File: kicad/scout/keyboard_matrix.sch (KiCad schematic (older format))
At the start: 17 parts, among them SW10 SPST, SW11 SPST, SW12 SPST, SW13 SPST, SW14 SPST, SW15 SPST, SW16 SPST, SW17 SPST, SW18 SPST, SW2 SPST, SW3 SPST, SW4 SPST, SW5 SPST, SW6 SPST, SW7 SPST, SW8 SPST, SW9 SPST

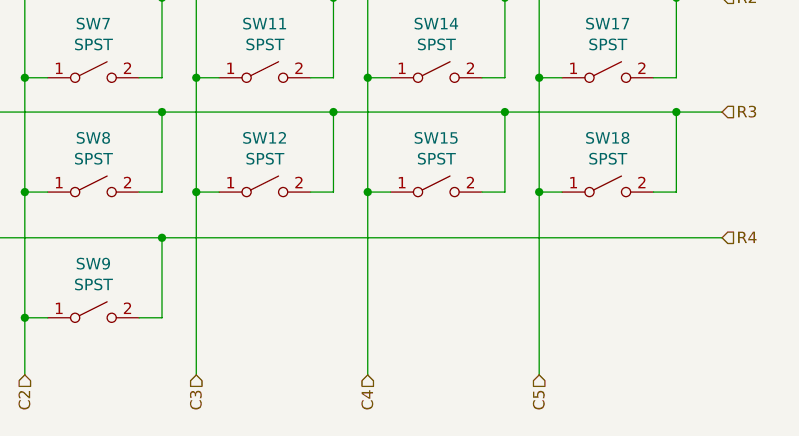
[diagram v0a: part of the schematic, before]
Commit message: PCB rev _b (private B)
* Increase mount length
* Move, right-angle (same footprint), flip to front, and reverse switch
* Move RGB LED, fix pin order, switch to easier footprint, and label GND
* Move FTDI and headphone jack for better exposure
* Add ICSP header
* Expose remaining ATMEGA pins and matrix buttons for hacking
* Add license, website, and plead
* Test SVG silkscreens -- fun!
* Mark relief hole to show which side it goes in
* Polarize C3 (amp gain) from ceramic to electrolytic
* Reverse volume direction
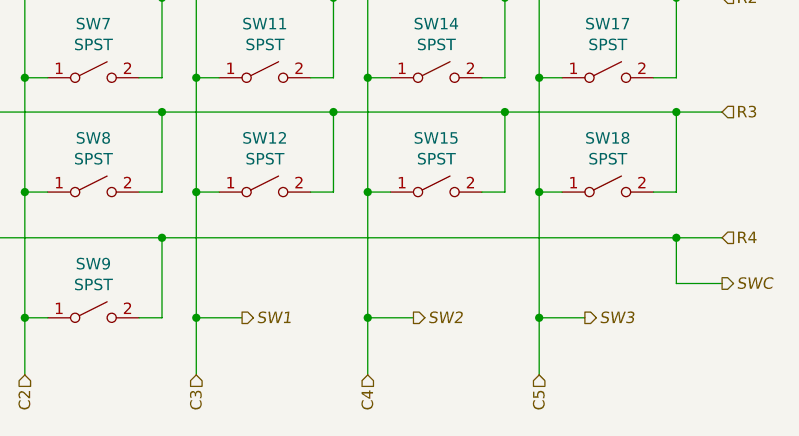
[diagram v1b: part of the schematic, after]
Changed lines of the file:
@@
 Connection ~ 7000 3850
 Wire Wire Line
-	4750 4400 7200 4400
+	4750 4400 7000 4400
 Connection ~ 4750 4400
 Wire Wire Line
@@
 Connection ~ 4150 4750
 Wire Wire Line
-	4900 4200 4900 5000
+	4900 4200 4900 4750
 Connection ~ 4900 4200
 Wire Wire Line
-	5650 4200 5650 5000
+	5650 4200 5650 4750
 Connection ~ 5650 4200
 Wire Wire Line
-	6400 4200 6400 5000
+	6400 4200 6400 4750
 Connection ~ 6400 4200
 Text HLabel 6400 5000 3    50   Input ~ 0
 C5
+Text HLabel 5100 4750 2    50   Output Italic 0
+SW1
+Text HLabel 5850 4750 2    50   Output Italic 0
+SW2
+Text HLabel 6600 4750 2    50   Output Italic 0
+SW3
+Wire Wire Line
+	4900 4750 5100 4750
+Connection ~ 4900 4750
+Wire Wire Line
+	4900 4750 4900 5000
+Wire Wire Line
+	5650 4750 5850 4750
+Connection ~ 5650 4750
+Wire Wire Line
+	5650 4750 5650 5000
+Wire Wire Line
+	6600 4750 6400 4750
+Connection ~ 6400 4750
+Wire Wire Line
+	6400 4750 6400 5000
+Text HLabel 7200 4600 2    50   Output Italic 0
+SWC
+Wire Wire Line
+	7000 4400 7000 4600
+Wire Wire Line
+	7000 4600 7200 4600
+Connection ~ 7000 4400
+Wire Wire Line
+	7000 4400 7200 4400
 $EndSCHEMATC

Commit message: Add schematic sheet corner text
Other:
- note added: "2020/07/16"
- note added: "A"
- note added: "Scout keyboard matrix"
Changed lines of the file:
@@
 Wire Wire Line
 	7000 4400 7200 4400
+Text Notes 7450 7500 0    50   ~ 0
+Scout keyboard matrix
+Text Notes 10600 7650 0    50   ~ 0
+A
+Text Notes 8150 7650 0    50   ~ 0
+2020/07/16
 $EndSCHEMATC

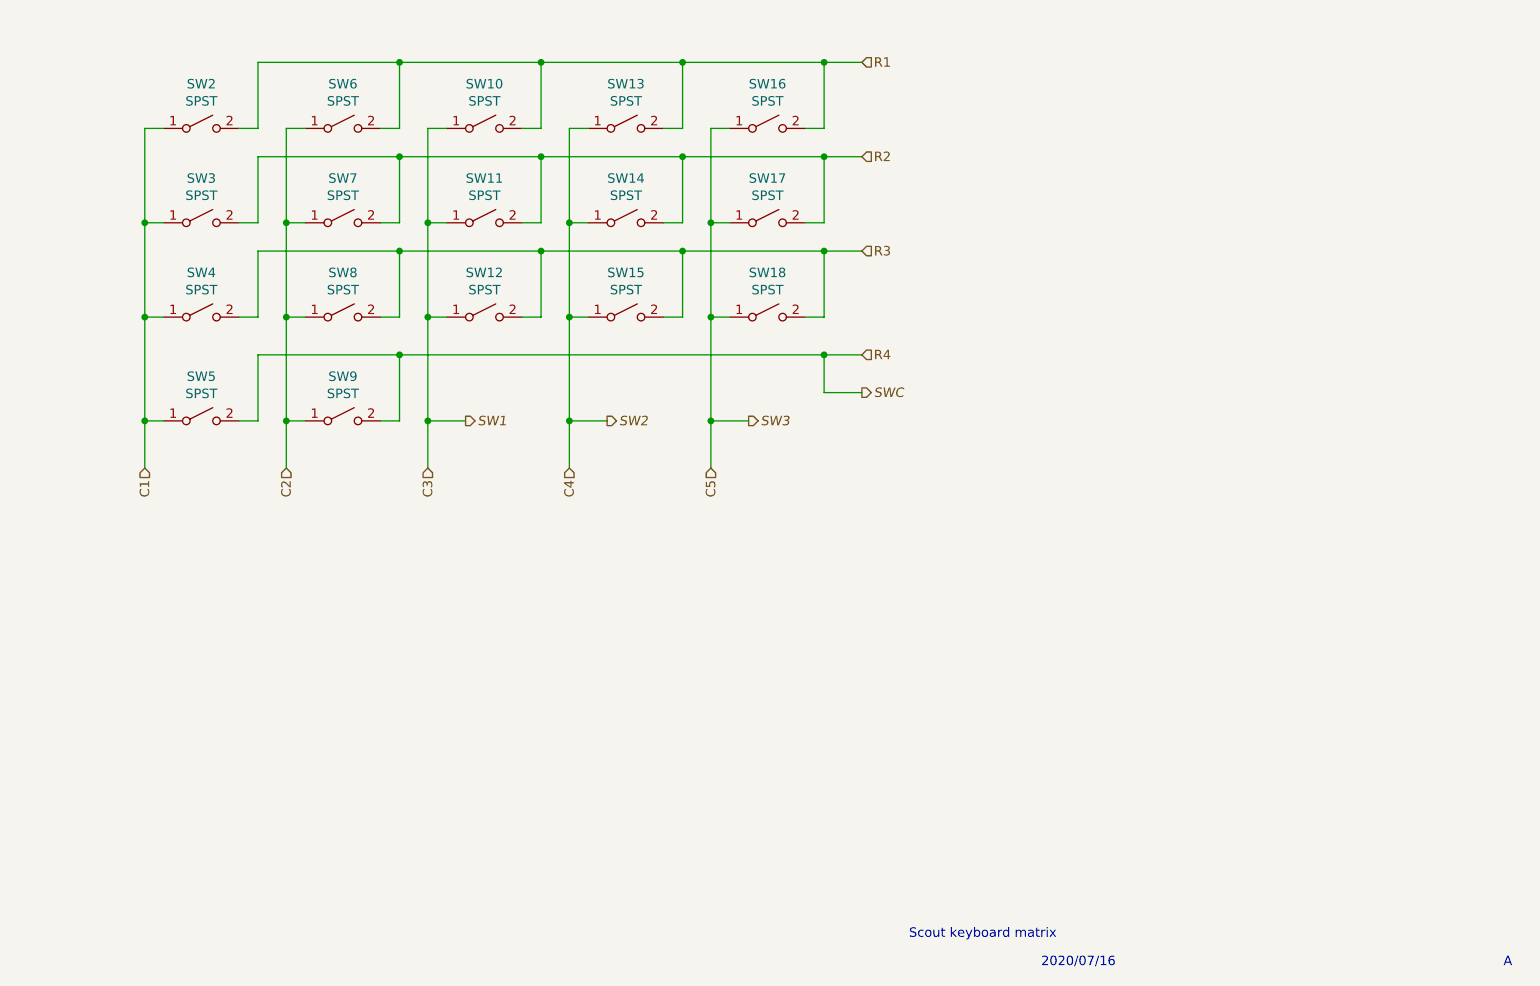
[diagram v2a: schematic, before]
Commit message: START Revise schematics
* Add all key switches with new diodes
* Swap pins 9 and 11 (re: MozziScout)
* Add two analog input pots
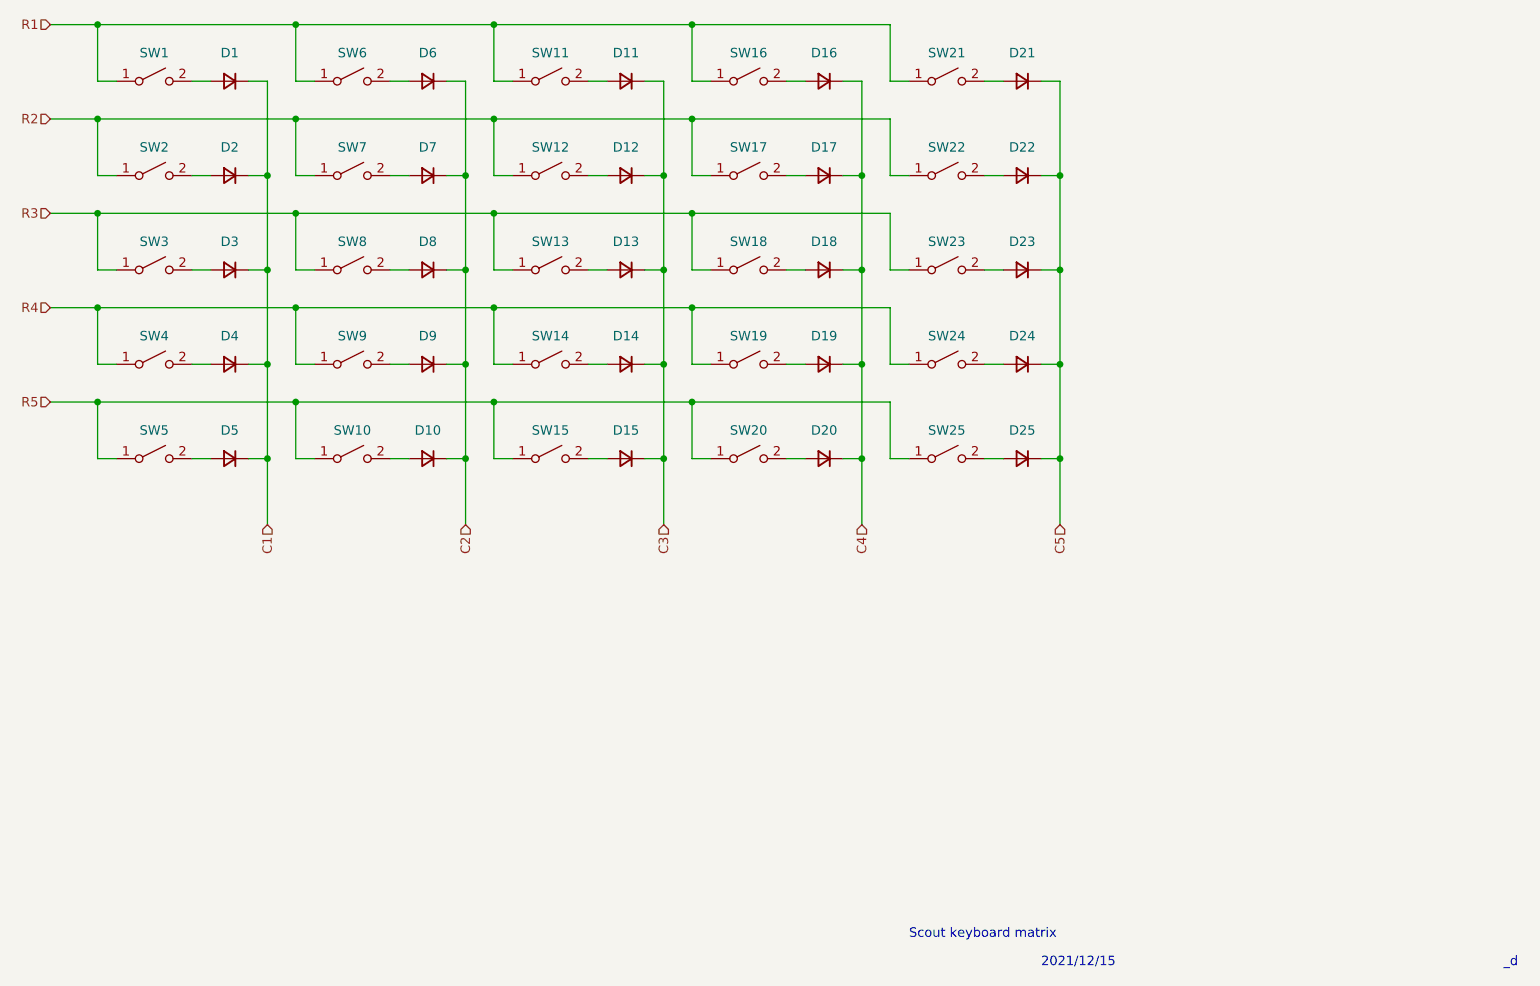
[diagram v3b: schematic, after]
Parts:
- added D1, D10, D11, D12, D13, D14, D15, D16, D17, D18, D19, D2, D20, D21, D22, D23, D24, D25, D3, D4, D5, D6, D7, D8, D9: D, symbol Device:D_Small
- added SW1, SW19, SW20, SW21, SW22, SW23, SW24, SW25: SPST, Button_Switch_THT:SW_PUSH_6mm, symbol Switch:SW_SPST
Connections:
- net C1: now also D1.1 (K), D2.1 (K), D3.1 (K), D4.1 (K), D5.1 (K); no longer SW2.1 (A), SW3.1 (A), SW4.1 (A), SW5.1 (A)
- net C2: now also D10.1 (K), D6.1 (K), D7.1 (K), D8.1 (K), D9.1 (K); no longer SW6.1 (A), SW7.1 (A), SW8.1 (A), SW9.1 (A)
- net C3: now also D11.1 (K), D12.1 (K), D13.1 (K), D14.1 (K), D15.1 (K); no longer SW10.1 (A), SW11.1 (A), SW12.1 (A)
- net C4: now also D16.1 (K), D17.1 (K), D18.1 (K), D19.1 (K), D20.1 (K); no longer SW13.1 (A), SW14.1 (A), SW15.1 (A)
- net C5: now also D21.1 (K), D22.1 (K), D23.1 (K), D24.1 (K), D25.1 (K); no longer SW16.1 (A), SW17.1 (A), SW18.1 (A)
- net R1: now also SW11.1 (A), SW16.1 (A), SW6.1 (A), SW1.1 (A), SW21.1 (A); no longer SW10.2 (B), SW13.2 (B), SW16.2 (B), SW2.2 (B), SW6.2 (B)
- net R2: now also SW12.1 (A), SW17.1 (A), SW2.1 (A), SW7.1 (A), SW22.1 (A); no longer SW11.2 (B), SW14.2 (B), SW17.2 (B), SW3.2 (B), SW7.2 (B)
- net R3: now also SW13.1 (A), SW18.1 (A), SW3.1 (A), SW8.1 (A), SW23.1 (A); no longer SW12.2 (B), SW15.2 (B), SW18.2 (B), SW4.2 (B), SW8.2 (B)
- net R4: now also SW14.1 (A), SW4.1 (A), SW9.1 (A), SW19.1 (A), SW24.1 (A); no longer SW5.2 (B), SW9.2 (B)
- new net: D1.2 (A), SW1.2 (B)
- new net: D6.2 (A), SW6.2 (B)
- new net: D11.2 (A), SW11.2 (B)
- new net: D16.2 (A), SW16.2 (B)
- new net: D21.2 (A), SW21.2 (B)
- new net: D2.2 (A), SW2.2 (B)
- new net: D7.2 (A), SW7.2 (B)
- new net: D12.2 (A), SW12.2 (B)
- new net: D17.2 (A), SW17.2 (B)
- new net: D22.2 (A), SW22.2 (B)
- new net: D3.2 (A), SW3.2 (B)
- new net: D8.2 (A), SW8.2 (B)
- new net: D13.2 (A), SW13.2 (B)
- new net: D18.2 (A), SW18.2 (B)
- new net: D23.2 (A), SW23.2 (B)
- new net: D4.2 (A), SW4.2 (B)
- new net: D9.2 (A), SW9.2 (B)
- new net: D14.2 (A), SW14.2 (B)
- new net: D19.2 (A), SW19.2 (B)
- new net: D24.2 (A), SW24.2 (B)
- new net: D5.2 (A), SW5.2 (B)
- new net: D10.2 (A), SW10.2 (B)
- new net: D15.2 (A), SW15.2 (B)
- new net: D20.2 (A), SW20.2 (B)
- new net: D25.2 (A), SW25.2 (B)
- new net R5: SW10.1 (A), SW15.1 (A), SW20.1 (A), SW25.1 (A), SW5.1 (A)
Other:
- note added: "2021/12/15"
- note added: "_d"
- note removed: "2020/07/16"
- note removed: "A"
